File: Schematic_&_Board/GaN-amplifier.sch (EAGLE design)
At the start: 77 parts, among them IC1 LT3080, Q1 MMBT3906LT1SMD, T1 IRL3714S, T2 IRL3714S, T3 IRL3714S, T4 IRL3714S, T5 BSP89, U1 TPS7A30XX, U2 HMC1099, U3 LT1783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

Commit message: Parts positioned
I've positioned the components. Now routing needs to happen.

DSB
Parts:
- added JP3: (no value), pinhead:PINHD-1X3
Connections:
- removed net N$32: L3.2, R29.I$1
- new net VL: R26.2, R29.V$2
- net +24V: now also JP3.1
- net -24V: now also JP3.3
- net GND: now also JP3.2
- net N$23: now also L3.2, R29.I$2; no longer R26.2, R29.V$1
- net N$27: now also R29.V$1; no longer R29.V$2
- net VDD: now also R29.I$1; no longer R29.I$2
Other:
- moved on the sheet: L1, L3, R29
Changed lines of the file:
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@@
 <part name="L2" library="jqi_passives" deviceset="L_FERRITE_SMD" device="LFERRITE_0402" value="5.6n"/>
 <part name="L3" library="coilcraft-jqi" deviceset="1008AF-XX" device="" value="0.9u"/>
+<part name="JP3" library="pinhead" deviceset="PINHD-1X3" device=""/>
+<part name="P+11" library="supply1" deviceset="+24V" device=""/>
+<part name="P-2" library="supply1" deviceset="-24V" device=""/>
+<part name="GND18" library="supply1" deviceset="GND" device=""/>
 </parts>
 <sheets>
@@
 <instance part="R8" gate="G$1" x="25.4" y="201.93" rot="R90"/>
 <instance part="GND6" gate="1" x="0" y="59.69"/>
-<instance part="L1" gate="G$1" x="86.36" y="220.98" rot="R90"/>
+<instance part="L1" gate="G$1" x="81.28" y="220.98" rot="R90"/>
 <instance part="U2" gate="G$1" x="40.64" y="220.98"/>
 <instance part="T1" gate="G$1" x="102.87" y="127" rot="R90"/>
@@
 <instance part="R28" gate="G$1" x="130.81" y="208.28" rot="R180"/>
 <instance part="X3" gate="G$1" x="152.4" y="200.66" rot="R180"/>
-<instance part="R29" gate="G$1" x="71.12" y="189.23" rot="R270"/>
+<instance part="R29" gate="G$1" x="67.31" y="189.23" rot="R180"/>
 <instance part="C23" gate="G$1" x="104.14" y="220.98" rot="MR90"/>
 <instance part="C24" gate="G$1" x="-7.62" y="220.98" rot="MR90"/>
@@
 <instance part="C26" gate="G$1" x="0" y="212.09" rot="MR0"/>
 <instance part="L2" gate="G$1" x="12.7" y="220.98"/>
-<instance part="L3" gate="G$1" x="66.04" y="208.28"/>
+<instance part="L3" gate="G$1" x="62.23" y="208.28"/>
+<instance part="JP3" gate="A" x="-11.43" y="181.61"/>
+<instance part="P+11" gate="1" x="-20.32" y="189.23"/>
+<instance part="P-2" gate="1" x="-20.32" y="173.99"/>
+<instance part="GND18" gate="1" x="-27.94" y="176.53"/>
 </instances>
 <busses>
@@
 <junction x="-12.7" y="214.63"/>
 </segment>
+<segment>
+<pinref part="GND18" gate="1" pin="GND"/>
+<pinref part="JP3" gate="A" pin="2"/>
+<wire x1="-27.94" y1="179.07" x2="-27.94" y2="181.61" width="0.1524" layer="91"/>
+<wire x1="-27.94" y1="181.61" x2="-13.97" y2="181.61" width="0.1524" layer="91"/>
+</segment>
 </net>
 <net name="N$15" class="0">
@@
 <junction x="-38.1" y="86.36"/>
 </segment>
+<segment>
+<pinref part="JP3" gate="A" pin="3"/>
+<pinref part="P-2" gate="1" pin="-24V"/>
+<wire x1="-13.97" y1="179.07" x2="-20.32" y2="179.07" width="0.1524" layer="91"/>
+<wire x1="-20.32" y1="179.07" x2="-20.32" y2="176.53" width="0.1524" layer="91"/>
+</segment>
 </net>
 <net name="+24V" class="0">
@@
 <wire x1="143.51" y1="135.89" x2="143.51" y2="129.54" width="0.1524" layer="91"/>
 <wire x1="143.51" y1="129.54" x2="140.97" y2="129.54" width="0.1524" layer="91"/>
+</segment>
+<segment>
+<pinref part="JP3" gate="A" pin="1"/>
+<pinref part="P+11" gate="1" pin="+24V"/>
+<wire x1="-13.97" y1="184.15" x2="-20.32" y2="184.15" width="0.1524" layer="91"/>
+<wire x1="-20.32" y1="184.15" x2="-20.32" y2="186.69" width="0.1524" layer="91"/>
 </segment>
 </net>
@@
 <wire x1="64.77" y1="166.37" x2="64.77" y2="160.02" width="0.1524" layer="91"/>
 <junction x="64.77" y="166.37"/>
-<pinref part="R29" gate="G$1" pin="I$2"/>
-<wire x1="64.77" y1="179.07" x2="64.77" y2="184.15" width="0.1524" layer="91"/>
-<wire x1="64.77" y1="184.15" x2="66.04" y2="184.15" width="0.1524" layer="91"/>
-<junction x="64.77" y="179.07"/>
+</segment>
+<segment>
+<pinref part="R29" gate="G$1" pin="I$1"/>
+<wire x1="72.39" y1="194.31" x2="72.39" y2="200.66" width="0.1524" layer="91"/>
+<label x="72.39" y="195.58" size="1.778" layer="95" rot="R90"/>
 </segment>
 </net>
@@
 </segment>
 </net>
-<net name="N$27" class="0">
-<segment>
-<pinref part="R29" gate="G$1" pin="V$2"/>
-<pinref part="R25" gate="G$1" pin="1"/>
-<wire x1="76.2" y1="184.15" x2="78.74" y2="184.15" width="0.1524" layer="91"/>
-</segment>
-</net>
 <net name="N$30" class="0">
 <segment>
@@
 <pinref part="L1" gate="G$1" pin="2"/>
 <pinref part="C23" gate="G$1" pin="2"/>
-<wire x1="93.98" y1="220.98" x2="96.52" y2="220.98" width="0.1524" layer="91"/>
+<wire x1="88.9" y1="220.98" x2="96.52" y2="220.98" width="0.1524" layer="91"/>
 <pinref part="C25" gate="G$1" pin="1"/>
 <wire x1="96.52" y1="220.98" x2="99.06" y2="220.98" width="0.1524" layer="91"/>
@@
 <pinref part="U2" gate="G$1" pin="OUT"/>
 <pinref part="L1" gate="G$1" pin="1"/>
-<wire x1="48.26" y1="220.98" x2="66.04" y2="220.98" width="0.1524" layer="91"/>
+<wire x1="48.26" y1="220.98" x2="62.23" y2="220.98" width="0.1524" layer="91"/>
 <pinref part="L3" gate="G$1" pin="1"/>
-<wire x1="66.04" y1="220.98" x2="78.74" y2="220.98" width="0.1524" layer="91"/>
-<wire x1="66.04" y1="215.9" x2="66.04" y2="220.98" width="0.1524" layer="91"/>
-<junction x="66.04" y="220.98"/>
+<wire x1="62.23" y1="220.98" x2="73.66" y2="220.98" width="0.1524" layer="91"/>
+<wire x1="62.23" y1="215.9" x2="62.23" y2="220.98" width="0.1524" layer="91"/>
+<junction x="62.23" y="220.98"/>
 </segment>
 </net>
@@
 </segment>
 </net>
-<net name="N$23" class="0">
-<segment>
-<pinref part="R29" gate="G$1" pin="V$1"/>
-<pinref part="R26" gate="G$1" pin="2"/>
-<wire x1="76.2" y1="194.31" x2="78.74" y2="194.31" width="0.1524" layer="91"/>
-</segment>
-</net>
 <net name="N$29" class="0">
 <segment>
@@
 </segment>
 </net>
-<net name="N$32" class="0">
-<segment>
-<pinref part="R29" gate="G$1" pin="I$1"/>
+<net name="N$23" class="0">
+<segment>
+<pinref part="R29" gate="G$1" pin="I$2"/>
 <pinref part="L3" gate="G$1" pin="2"/>
-<wire x1="66.04" y1="194.31" x2="66.04" y2="200.66" width="0.1524" layer="91"/>
-</segment>
-</net>
+<wire x1="62.23" y1="194.31" x2="62.23" y2="200.66" width="0.1524" layer="91"/>
+</segment>
+</net>
+<net name="N$27" class="0">
+<segment>
+<pinref part="R29" gate="G$1" pin="V$1"/>
+<pinref part="R25" gate="G$1" pin="1"/>
+<wire x1="72.39" y1="184.15" x2="78.74" y2="184.15" width="0.1524" layer="91"/>
+</segment>
+</net>
+<net name="VL" class="0">
+<segment>
+<pinref part="R29" gate="G$1" pin="V$2"/>
+<wire x1="62.23" y1="184.15" x2="62.23" y2="181.61" width="0.1524" layer="91"/>
+<wire x1="62.23" y1="181.61" x2="68.58" y2="181.61" width="0.1524" layer="91"/>
+<label x="63.5" y="181.61" size="1.778" layer="95"/>
+</segment>
+<segment>
+<pinref part="R26" gate="G$1" pin="2"/>
+<wire x1="78.74" y1="194.31" x2="78.74" y2="201.93" width="0.1524" layer="91"/>
+<label x="78.74" y="198.12" size="1.778" layer="95" rot="R90"/>
+</segment>
+</net>

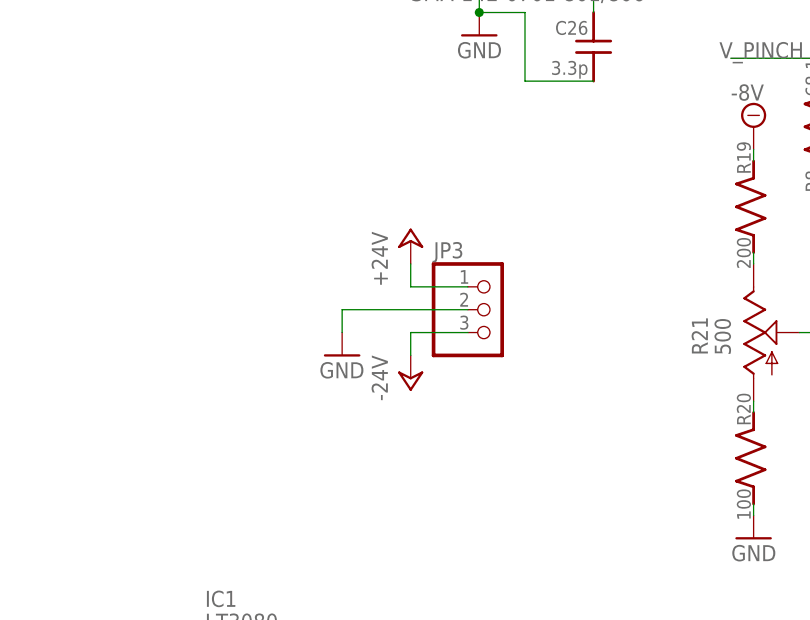
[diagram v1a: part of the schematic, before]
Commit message: Power Sequencing Layed Out
I've finished routing the power sequencing part of the PCB. Need to copy
positions of RF components from eval board gerber and design 50 Ohm
striplines.

DSB
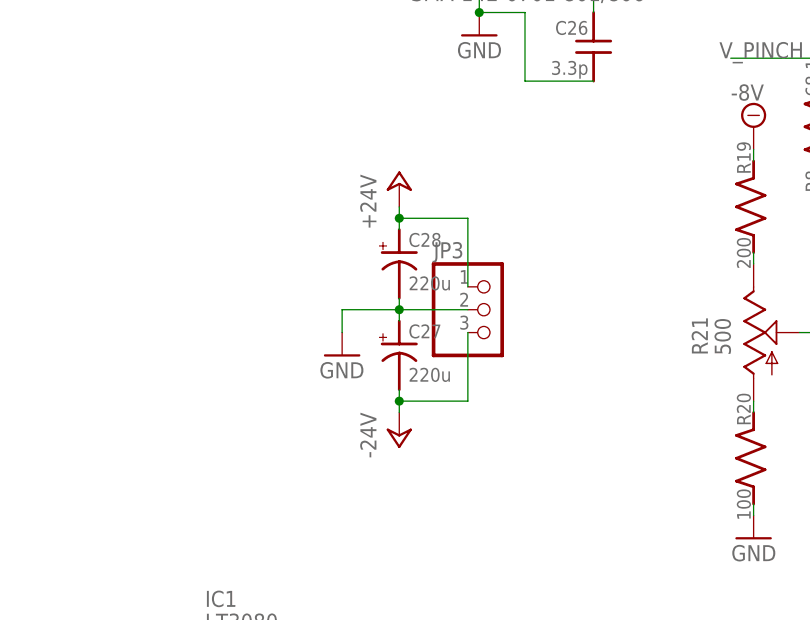
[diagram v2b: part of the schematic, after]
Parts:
- added C27, C28: 220u, jqi_passives:C_POL_SMDF
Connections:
- net +24V: now also C28.+
- net -24V: now also C27.-
- net GND: now also C27.+, C28.-
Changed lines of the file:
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@@
 <part name="P-2" library="supply1" deviceset="-24V" device=""/>
 <part name="GND18" library="supply1" deviceset="GND" device=""/>
+<part name="C27" library="jqi_passives" deviceset="C_POL_SMD" device="F" value="220u"/>
+<part name="C28" library="jqi_passives" deviceset="C_POL_SMD" device="F" value="220u"/>
 </parts>
 <sheets>
@@
 <instance part="L3" gate="G$1" x="62.23" y="208.28"/>
 <instance part="JP3" gate="A" x="-11.43" y="181.61"/>
-<instance part="P+11" gate="1" x="-20.32" y="189.23"/>
-<instance part="P-2" gate="1" x="-20.32" y="173.99"/>
+<instance part="P+11" gate="1" x="-21.59" y="195.58"/>
+<instance part="P-2" gate="1" x="-21.59" y="167.64"/>
 <instance part="GND18" gate="1" x="-27.94" y="176.53"/>
+<instance part="C27" gate="G$1" x="-21.59" y="177.8"/>
+<instance part="C28" gate="G$1" x="-21.59" y="187.96"/>
 </instances>
 <busses>
@@
 <pinref part="JP3" gate="A" pin="2"/>
 <wire x1="-27.94" y1="179.07" x2="-27.94" y2="181.61" width="0.1524" layer="91"/>
-<wire x1="-27.94" y1="181.61" x2="-13.97" y2="181.61" width="0.1524" layer="91"/>
+<wire x1="-27.94" y1="181.61" x2="-21.59" y2="181.61" width="0.1524" layer="91"/>
+<pinref part="C27" gate="G$1" pin="+"/>
+<wire x1="-21.59" y1="181.61" x2="-13.97" y2="181.61" width="0.1524" layer="91"/>
+<wire x1="-21.59" y1="180.34" x2="-21.59" y2="181.61" width="0.1524" layer="91"/>
+<junction x="-21.59" y="181.61"/>
+<pinref part="C28" gate="G$1" pin="-"/>
+<wire x1="-21.59" y1="181.61" x2="-21.59" y2="182.88" width="0.1524" layer="91"/>
 </segment>
 </net>
@@
 </segment>
 <segment>
+<pinref part="C27" gate="G$1" pin="-"/>
+<pinref part="P-2" gate="1" pin="-24V"/>
+<wire x1="-21.59" y1="172.72" x2="-21.59" y2="171.45" width="0.1524" layer="91"/>
 <pinref part="JP3" gate="A" pin="3"/>
-<pinref part="P-2" gate="1" pin="-24V"/>
-<wire x1="-13.97" y1="179.07" x2="-20.32" y2="179.07" width="0.1524" layer="91"/>
-<wire x1="-20.32" y1="179.07" x2="-20.32" y2="176.53" width="0.1524" layer="91"/>
+<wire x1="-21.59" y1="171.45" x2="-21.59" y2="170.18" width="0.1524" layer="91"/>
+<wire x1="-21.59" y1="171.45" x2="-13.97" y2="171.45" width="0.1524" layer="91"/>
+<wire x1="-13.97" y1="171.45" x2="-13.97" y2="179.07" width="0.1524" layer="91"/>
+<junction x="-21.59" y="171.45"/>
 </segment>
 </net>
@@
 </segment>
 <segment>
+<pinref part="C28" gate="G$1" pin="+"/>
+<pinref part="P+11" gate="1" pin="+24V"/>
+<wire x1="-21.59" y1="190.5" x2="-21.59" y2="191.77" width="0.1524" layer="91"/>
 <pinref part="JP3" gate="A" pin="1"/>
-<pinref part="P+11" gate="1" pin="+24V"/>
-<wire x1="-13.97" y1="184.15" x2="-20.32" y2="184.15" width="0.1524" layer="91"/>
-<wire x1="-20.32" y1="184.15" x2="-20.32" y2="186.69" width="0.1524" layer="91"/>
+<wire x1="-21.59" y1="191.77" x2="-21.59" y2="193.04" width="0.1524" layer="91"/>
+<wire x1="-21.59" y1="191.77" x2="-13.97" y2="191.77" width="0.1524" layer="91"/>
+<wire x1="-13.97" y1="191.77" x2="-13.97" y2="184.15" width="0.1524" layer="91"/>
+<junction x="-21.59" y="191.77"/>
 </segment>
 </net>

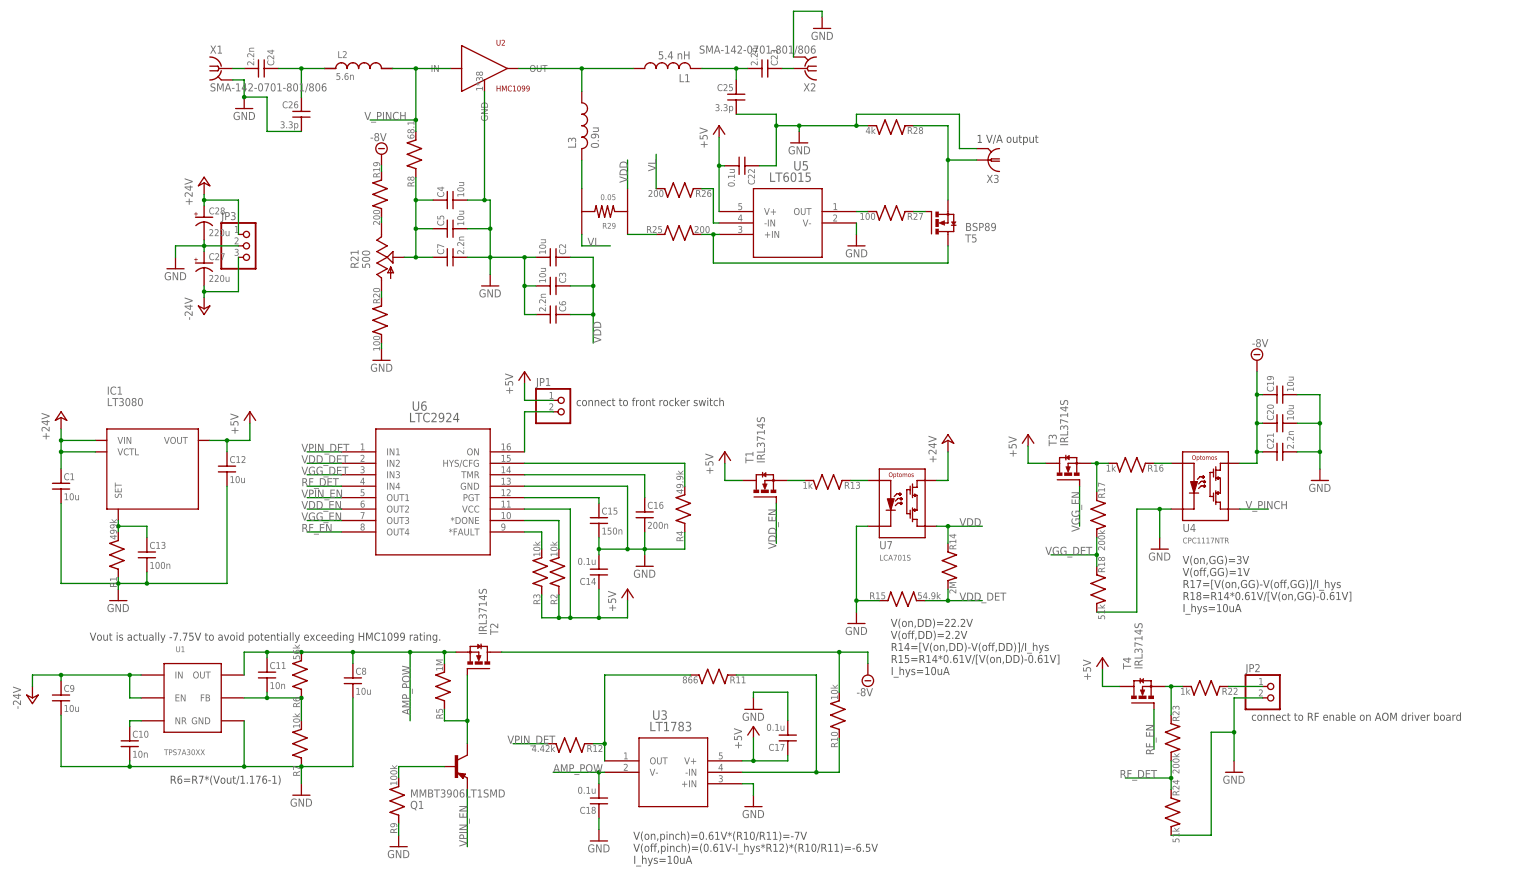
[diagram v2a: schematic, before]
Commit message: Add VGG Buffer
Added buffer for the GaN amp gate voltage. Also made progress on RF
layout.

DSB
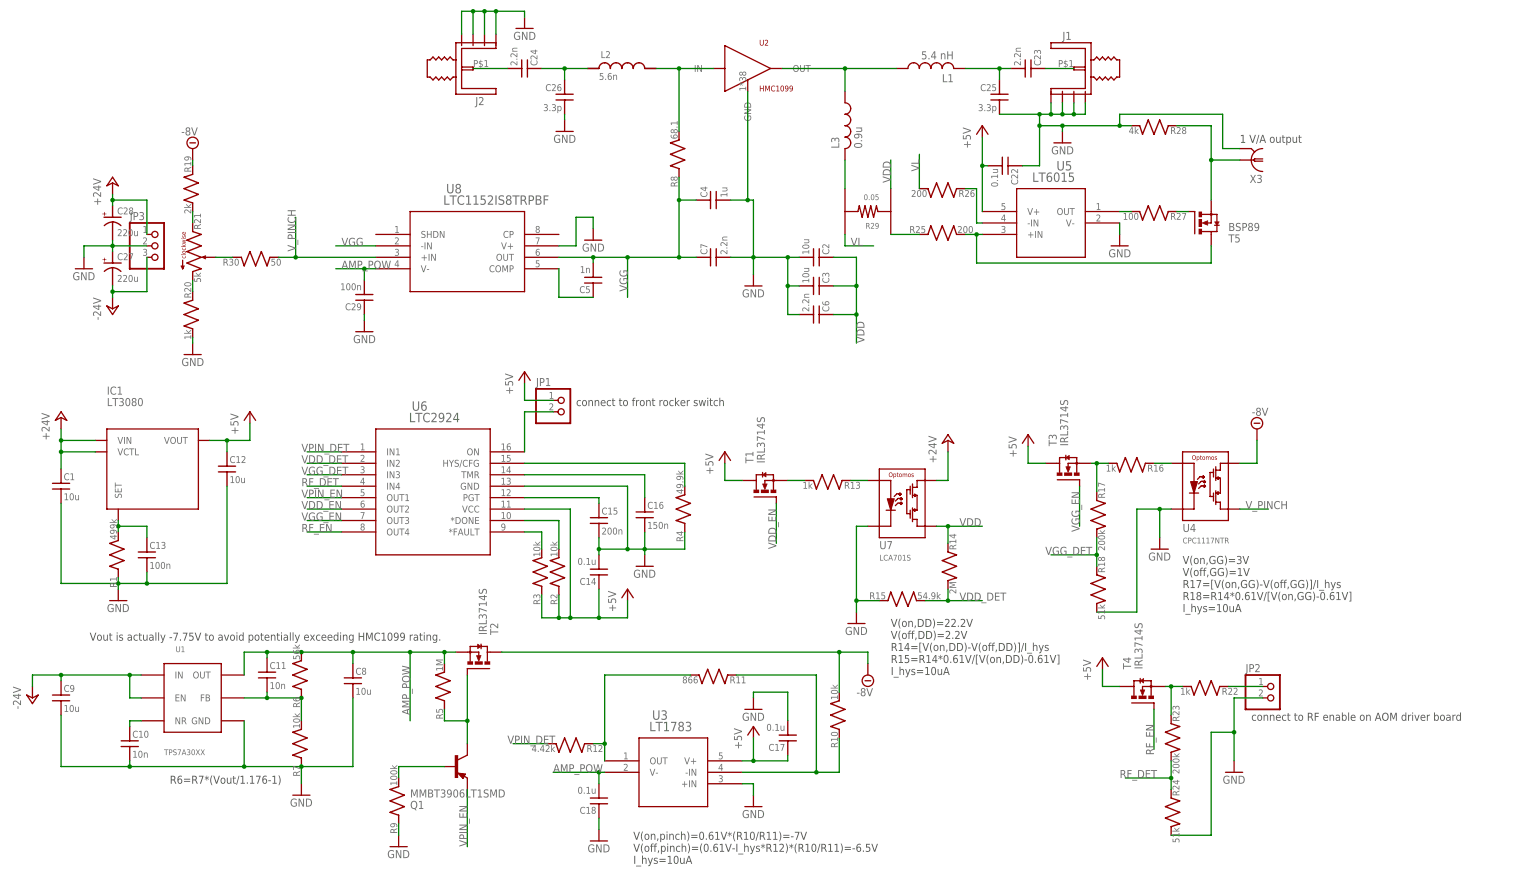
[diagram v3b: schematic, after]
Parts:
- removed C19, C20: 10u, jqi_passives:C_MLCC_SMDCMLCC_1210
- removed C21: 2.2n, jqi_passives:C_MLCC_SMDCMLCC_0603
- removed X1, X2: SMA-142-0701-801/806, con-coax:SMA-142-0701-801/806
- added C29: 100n, jqi_passives:C_MLCC_SMDCMLCC_0603
- added J1, J2: JOHNSON_SMA_EDGE_LAUNCH_142-0701-851, connector-jqi:JOHNSON_SMA_EDGE_LAUNCH_142-0701-851
- added R30: 50, jqi_passives:R_SMDR0603
- added U8: LTC1152IS8TRPBF, linear-technology-jqi:LTC1152IS8TRPBF
- C15: value 150n -> 200n
- C16: value 200n -> 150n
- C4: value 10u -> 1u; device jqi_passives:C_MLCC_SMDCMLCC_1210 -> jqi_passives:C_MLCC_SMDCMLCC_0603
- C5: value 10u -> 1n; device jqi_passives:C_MLCC_SMDCMLCC_1210 -> jqi_passives:C_MLCC_SMDCMLCC_0603
- R19: value 200 -> 2k
- R20: value 100 -> 1k
- R21: value 500 -> 5k; device rlc-jqi:BOURNS-3269P -> jqi_passives:R_TRIM
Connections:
- removed net N$18: C4.1, C5.1, C7.1, R21.2, R8.1
- new net N$32: C5.1, U8.COMP
- new net N$36: R21.2, R30.1
- new net VGG: C4.1, C5.2, C7.1, R8.1, U8.-IN, U8.OUT
- new net V_GATE: L2.2, R8.2, U2.IN
- net -8V: no longer C19.1, C20.1, C21.1
- net AMP_POW: now also C29.2, U8.V-
- net GND: now also C29.1, J1.GND, J1.GND1, J1.GND2, J1.GND3, J2.GND, J2.GND1, J2.GND2, J2.GND3, U8.V+; no longer C19.2, C20.2, C21.2, C5.2, X1.2, X2.2
- net N$19: now also R21.1; no longer R21.3
- net N$20: now also R21.3; no longer R21.1
- net N$30: now also J1.P$1; no longer X2.1
- net N$31: now also J2.P$1; no longer X1.1
- net V_PINCH: now also R30.2, U8.+IN; no longer L2.2, R8.2, U2.IN
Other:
- moved on the sheet: C2, C22, C23, C24, C25, C26, C27, C28, C3, C4, C5, C6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
